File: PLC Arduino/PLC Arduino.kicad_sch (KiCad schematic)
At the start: 212 parts, among them J1 Screw_Terminal_01x12, J10 Conn_01x03_Socket, J11 Conn_01x05_Socket, J12 Conn_01x03_Socket, J13 Conn_01x05_Socket, J14 Screw_Terminal_01x08, J15 Screw_Terminal_01x08, J2 Screw_Terminal_01x12, J3 Screw_Terminal_01x12, J4 Screw_Terminal_01x12, J5 USB_B_Micro, J6 Conn_01x04_Socket, J7 Conn_01x03_Socket, J8 Conn_01x02_Socket, J9 Conn_01x02_Socket, K1 SANYOU_SRD_Form_C, K2 SANYOU_SRD_Form_C, K3 SANYOU_SRD_Form_C, K5 SANYOU_SRD_Form_C, Q1 Q_NMOS_Depletion_GSD, Q10 BSS138, Q2 Q_NMOS_Depletion_GSD, Q3 Q_NMOS_Depletion_GSD, Q4 Q_NMOS_Depletion_GSD, Q5 Q_NMOS_Depletion_GSD, Q6 Q_NMOS_Depletion_GSD, Q7 Q_NMOS_Depletion_GSD, Q8 Q_NMOS_Depletion_GSD, Q9 BSS138, SW1 SW_Push, SW2 SW_Push, U1 PC817, U10 PC817, U11 PC817, U12 PC817, U13 PC817, U14 PC817, U15 PC817, U16 PC817, U18 ADS1115IDGS, U2 PC817, U22 ISO1540, U23 ESP32-WROOM-32, U24 CH340C, U25 MAX485E, U26 MAX485E, U27 TPL5010, U28 B0505S-2WR3, U29 LM2596S-5, U3 PC817, U30 AMS1117-3.3, U31 AMS1117-3.3, U32 74HC595, U33 74HC595, U34 74HC4051, U4 PC817, U5 PC817, U6 PC817, U7 PC817, U8 PC817, U9 PC817

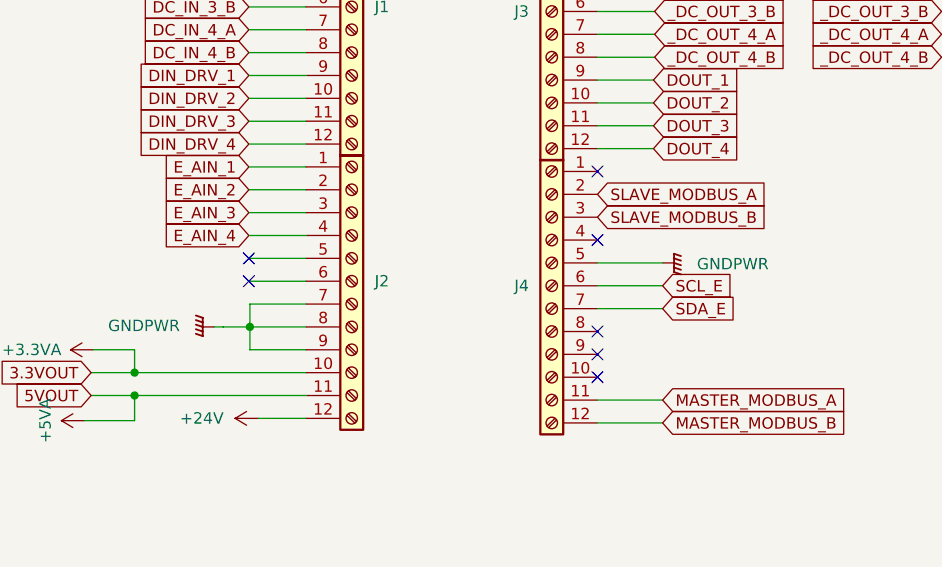
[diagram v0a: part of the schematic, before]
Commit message: Done PCB Layout PLC Board
To DO:

Review from Nes
Round Corners of Strobe and PLC
Proper Labels PLC Board
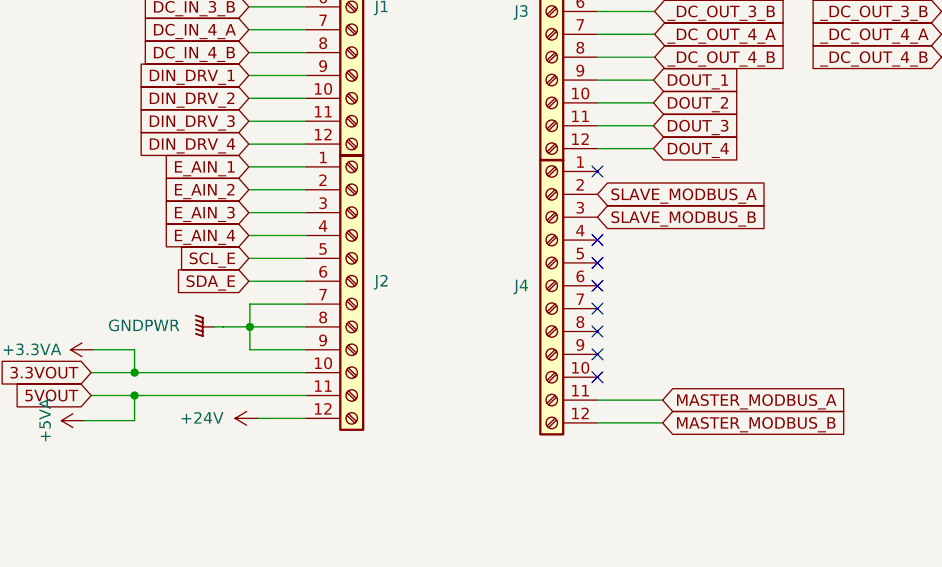
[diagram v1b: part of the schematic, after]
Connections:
- net GNDPWR: no longer J4.5 (Pin_5)
- net SCL_E: now also J2.5 (Pin_5); no longer J4.6 (Pin_6)
- net SDA_E: now also J2.6 (Pin_6); no longer J4.7 (Pin_7)
- no-connect marks 40 -> 41
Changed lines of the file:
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@@
 	)
 	(no_connect
+		(at 614.553 82.804)
+	)
+	(no_connect
+		(at 614.553 77.724)
+	)
+	(no_connect
 		(at 478.79 411.48)
 	)
@@
 	)
 	(no_connect
-		(at 575.818 77.216)
+		(at 614.553 85.344)
 	)
 	(no_connect
-		(at 614.553 85.344)
+		(at 614.553 80.264)
 	)
 	(no_connect
@@
 	)
 	(no_connect
-		(at 575.818 79.756)
-	)
-	(no_connect
 		(at 368.173 454.66)
 	)
@@
 	(wire
 		(pts
-			(xy 614.553 77.724) (xy 621.792 77.724)
-		)
-		(stroke
-			(width 0)
-			(type default)
-		)
-	)
-	(wire
-		(pts
 			(xy 349.504 183.134) (xy 351.536 183.134)
 		)
@@
 	(wire
 		(pts
-			(xy 614.553 82.804) (xy 621.792 82.804)
-		)
-		(stroke
-			(width 0)
-			(type default)
-		)
-	)
-	(wire
-		(pts
 			(xy 65.278 87.884) (xy 68.326 87.884)
 		)
@@
 	(wire
 		(pts
-			(xy 614.553 80.264) (xy 621.792 80.264)
-		)
-		(stroke
-			(width 0)
-			(type default)
-		)
-	)
-	(wire
-		(pts
 			(xy 697.738 335.788) (xy 697.738 337.693)
 		)
@@
 		)
 	)
+	(global_label "SCL_E"
+		(shape input)
+		(at 575.818 77.216 180)
+		(fields_autoplaced yes)
+		(effects
+			(font
+				(size 1.27 1.27)
+			)
+			(justify right)
+		)
+		(property "Intersheetrefs" "${INTERSHEET_REFS}"
+			(at 567.2086 77.216 0)
+			(effects
+				(font
+					(size 1.27 1.27)
+				)
+				(justify right)
+				(hide yes)
+			)
+		)
+	)
 	(global_label "DOUT_DRV_4"
 		(shape input)
@@
 		)
 	)
-	(global_label "SCL_E"
-		(shape input)
-		(at 621.792 80.264 0)
-		(fields_autoplaced yes)
-		(effects
-			(font
-				(size 1.27 1.27)
-			)
-			(justify left)
-		)
-		(property "Intersheetrefs" "${INTERSHEET_REFS}"
-			(at 630.4014 80.264 0)
-			(effects
-				(font
-					(size 1.27 1.27)
-				)
-				(justify left)
-				(hide yes)
-			)
-		)
-	)
 	(global_label "_DC_OUT_3_A"
 		(shape input)
@@
 		)
 	)
+	(global_label "SDA_E"
+		(shape input)
+		(at 575.818 79.756 180)
+		(fields_autoplaced yes)
+		(effects
+			(font
+				(size 1.27 1.27)
+			)
+			(justify right)
+		)
+		(property "Intersheetrefs" "${INTERSHEET_REFS}"
+			(at 567.1481 79.756 0)
+			(effects
+				(font
+					(size 1.27 1.27)
+				)
+				(justify right)
+				(hide yes)
+			)
+		)
+	)
 	(global_label "DC_IN_4_A"
 		(shape input)
@@
 		)
 	)
-	(global_label "SDA_E"
-		(shape input)
-		(at 621.792 82.804 0)
-		(fields_autoplaced yes)
-		(effects
-			(font
-				(size 1.27 1.27)
-			)
-			(justify left)
-		)
-		(property "Intersheetrefs" "${INTERSHEET_REFS}"
-			(at 630.4619 82.804 0)
-			(effects
-				(font
-					(size 1.27 1.27)
-				)
-				(justify left)
-				(hide yes)
-			)
-		)
-	)
 	(global_label "DIN_DRV_1"
 		(shape input)
@@
 					(unit 1)
 				)
-			)
-		)
-	)
-	(symbol
-		(lib_id "power:GNDPWR")
-		(at 621.792 77.724 90)
-		(unit 1)
-		(exclude_from_sim no)
-		(in_bom yes)
-		(on_board yes)
-		(dnp no)
-		(fields_autoplaced yes)
-		(property "Reference" "#PWR075"
-			(at 626.872 77.724 0)
-			(effects
-				(font
-					(size 1.27 1.27)
-				)
-				(hide yes)
-			)
-		)
-		(property "Value" "GNDPWR"
-			(at 625.602 77.8509 90)
-			(effects
-				(font
-					(size 1.27 1.27)
-				)
-				(justify right)
-			)
-		)
-		(property "Footprint" ""
-			(at 623.062 77.724 0)
-			(effects
-				(font
-					(size 1.27 1.27)
-				)
-				(hide yes)
-			)
-		)
-		(property "Datasheet" ""
-			(at 623.062 77.724 0)
-			(effects
-				(font
-					(size 1.27 1.27)
-				)
-				(hide yes)
-			)
-		)
-		(property "Description" "Power symbol creates a global label with name \"GNDPWR\" , global ground"
-			(at 621.792 77.724 0)
-			(effects
-				(font
-					(size 1.27 1.27)
-				)
-				(hide yes)
-			)
-		)
-		(pin "1"
-		)
-		(instances
-			(project "PLC Arduino"
-				(path "/ce68e045-3b24-4b1f-b4c3-20bce3f1de80"
-					(reference "#PWR075")
-					(unit 1)
-				)
